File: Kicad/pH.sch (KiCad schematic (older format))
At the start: 6 parts, among them U1 MCP6241

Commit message: Ready for Rev3 First layout review
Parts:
- removed TP17, TP18: CONN_1, symbol CONN_1
- added C3: .1, ~, symbol C
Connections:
- net AGND: now also C3.2
- net V+_WallWart renamed V+_Clean
- net V+_Clean: now also C3.1
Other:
- note added: "Added .1uF"
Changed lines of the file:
@@
 $Descr A4 11693 8268
 encoding utf-8
-Sheet 7 7
+Sheet 6 7
 Title ""
-Date "11 oct 2014"
+Date "18 oct 2014"
 Rev ""
 Comp ""
@@
 Comment4 ""
 $EndDescr
-Text HLabel 3900 2400 0    60   Input ~ 0
+Text HLabel 1400 1200 0    60   Input ~ 0
 V+_WallWart
 Text HLabel 1350 3200 0    60   Input ~ 0
@@
 	1    0    0    -1
 $EndComp
-Wire Wire Line
-	3900 2900 3900 2400
 $Comp
 L CONN_1 TP1
@@
 Wire Wire Line
 	7450 3200 7450 3600
-Text HLabel 7450 2450 0    60   Input ~ 0
-V+_WallWart
-Wire Wire Line
-	7450 2700 7450 2450
 Text HLabel 5700 3100 2    60   Input ~ 0
 pH_Probe_V
@@
 Text HLabel 8600 3400 2    60   Input ~ 0
 pH_Probe_GND
-$Comp
-L CONN_1 TP18
-U 1 1 540C941C
-P 8500 2900
-F 0 "TP18" H 8580 2900 40  0000 L CNN
-F 1 "CONN_1" H 8500 2955 30  0001 C CNN
-F 2 "" H 8500 2900 60  0000 C CNN
-F 3 "" H 8500 2900 60  0000 C CNN
-	1    8500 2900
-	1    0    0    -1
-$EndComp
 Wire Wire Line
 	8050 1900 8050 3400
-$Comp
-L CONN_1 TP17
-U 1 1 540C9446
-P 5150 2750
-F 0 "TP17" H 5230 2750 40  0000 L CNN
-F 1 "CONN_1" H 5150 2805 30  0001 C CNN
-F 2 "" H 5150 2750 60  0000 C CNN
-F 3 "" H 5150 2750 60  0000 C CNN
-	1    5150 2750
-	0    -1   -1   0
-$EndComp
-Wire Wire Line
-	5150 2900 5150 3100
-Connection ~ 5150 3100
 Wire Wire Line
 	8050 1900 7950 1900
@@
 Connection ~ 7450 3400
 Connection ~ 8050 3400
+$Comp
+L C C3
+U 1 1 5441038F
+P 2000 1650
+F 0 "C3" H 2000 1750 40  0000 L CNN
+F 1 ".1" H 2006 1565 40  0000 L CNN
+F 2 "~" H 2038 1500 30  0000 C CNN
+F 3 "~" H 2000 1650 60  0000 C CNN
+	1    2000 1650
+	1    0    0    -1
+$EndComp
 Wire Wire Line
-	8350 2900 8350 3400
-Connection ~ 8350 3400
+	5950 2450 7450 2450
+Text Notes 1850 1050 0    60   ~ 0
+Added .1uF
+Wire Wire Line
+	1400 1200 2750 1200
+Wire Wire Line
+	2000 1450 2000 1200
+Connection ~ 2000 1200
+$Comp
+L AGND #PWR09
+U 1 1 5441062F
+P 2000 2050
+F 0 "#PWR09" H 2000 2050 40  0001 C CNN
+F 1 "AGND" H 2000 1980 50  0000 C CNN
+F 2 "" H 2000 2050 60  0000 C CNN
+F 3 "" H 2000 2050 60  0000 C CNN
+	1    2000 2050
+	1    0    0    -1
+$EndComp
+Wire Wire Line
+	2000 1850 2000 2050
+Wire Wire Line
+	3900 2900 3900 2400
+Wire Wire Line
+	7450 2450 7450 2700
+Text GLabel 2750 1200 2    60   Output ~ 0
+V+_Clean
+Text GLabel 3900 2400 2    60   Output ~ 0
+V+_Clean
+Text GLabel 6100 2300 2    60   Output ~ 0
+V+_Clean
+Wire Wire Line
+	5950 2450 5950 2300
+Wire Wire Line
+	5950 2300 6100 2300
 $EndSCHEMATC

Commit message: updated based on feedback. Ready for second review
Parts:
- removed C3: .1, ~, symbol C
- added C10, C9: .1, ~, symbol C
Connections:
- net labels removed: V+_Clean
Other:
- note removed: "Added .1uF"
- moved on the sheet: R3, R4
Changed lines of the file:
@@
 Sheet 6 7
 Title ""
-Date "18 oct 2014"
+Date "21 oct 2014"
 Rev ""
 Comp ""
@@
 Comment4 ""
 $EndDescr
-Text HLabel 1400 1200 0    60   Input ~ 0
-V+_WallWart
 Text HLabel 1350 3200 0    60   Input ~ 0
 ph_ADC_IN+
-Wire Wire Line
-	3900 3500 3900 3750
 $Comp
 L R R4
 U 1 1 53D7D158
-P 7450 3850
-F 0 "R4" V 7530 3850 40  0000 C CNN
-F 1 "1K" V 7457 3851 40  0000 C CNN
-F 2 "~" V 7380 3850 30  0000 C CNN
-F 3 "~" H 7450 3850 30  0000 C CNN
-	1    7450 3850
+P 8400 3900
+F 0 "R4" V 8480 3900 40  0000 C CNN
+F 1 "1K" V 8407 3901 40  0000 C CNN
+F 2 "~" V 8330 3900 30  0000 C CNN
+F 3 "~" H 8400 3900 30  0000 C CNN
+	1    8400 3900
 	1    0    0    -1
 $EndComp
-Wire Wire Line
-	1350 3200 3450 3200
-Text HLabel 7950 1900 0    60   Input ~ 0
+Text HLabel 8900 1950 0    60   Input ~ 0
 pH_ADC_IN-
 $Comp
-L AGND #PWR07
+L AGND #PWR08
 U 1 1 53DCC7DA
 P 3900 3750
-F 0 "#PWR07" H 3900 3750 40  0001 C CNN
+F 0 "#PWR08" H 3900 3750 40  0001 C CNN
 F 1 "AGND" H 3900 3680 50  0000 C CNN
 F 2 "" H 3900 3750 60  0000 C CNN
@@
 L R R3
 U 1 1 53F37946
-P 7450 2950
-F 0 "R3" V 7530 2950 40  0000 C CNN
-F 1 "10K" V 7457 2951 40  0000 C CNN
-F 2 "~" V 7380 2950 30  0000 C CNN
-F 3 "~" H 7450 2950 30  0000 C CNN
-	1    7450 2950
+P 8400 3000
+F 0 "R3" V 8480 3000 40  0000 C CNN
+F 1 "10K" V 8407 3001 40  0000 C CNN
+F 2 "~" V 8330 3000 30  0000 C CNN
+F 3 "~" H 8400 3000 30  0000 C CNN
+	1    8400 3000
 	1    0    0    -1
 $EndComp
@@
 	0    -1   -1   0
 $EndComp
+Text HLabel 5700 3100 2    60   Input ~ 0
+pH_Probe_V
+$Comp
+L AGND #PWR09
+U 1 1 540C92AB
+P 8400 4450
+F 0 "#PWR09" H 8400 4450 40  0001 C CNN
+F 1 "AGND" H 8400 4380 50  0000 C CNN
+F 2 "" H 8400 4450 60  0000 C CNN
+F 3 "" H 8400 4450 60  0000 C CNN
+	1    8400 4450
+	1    0    0    -1
+$EndComp
+Text HLabel 9550 3450 2    60   Input ~ 0
+pH_Probe_GND
+$Comp
+L C C9
+U 1 1 54453E50
+P 3550 2700
+F 0 "C9" H 3550 2800 40  0000 L CNN
+F 1 ".1" H 3556 2615 40  0000 L CNN
+F 2 "~" H 3588 2550 30  0000 C CNN
+F 3 "~" H 3550 2700 60  0000 C CNN
+	1    3550 2700
+	1    0    0    -1
+$EndComp
+Text HLabel 3900 2300 0    60   Input ~ 0
+V+_WallWart
+$Comp
+L AGND #PWR010
+U 1 1 54453F29
+P 3550 2900
+F 0 "#PWR010" H 3550 2900 40  0001 C CNN
+F 1 "AGND" H 3550 2830 50  0000 C CNN
+F 2 "" H 3550 2900 60  0000 C CNN
+F 3 "" H 3550 2900 60  0000 C CNN
+	1    3550 2900
+	1    0    0    -1
+$EndComp
+Wire Wire Line
+	3900 3500 3900 3750
+Wire Wire Line
+	1350 3200 3450 3200
 Wire Wire Line
 	2350 3050 2350 3200
 Connection ~ 2350 3200
 Wire Wire Line
-	7450 3200 7450 3600
-Text HLabel 5700 3100 2    60   Input ~ 0
-pH_Probe_V
+	8400 3250 8400 3650
 Wire Wire Line
 	4150 3100 5700 3100
@@
 	4750 3300 4150 3300
 Connection ~ 2950 3200
+Wire Wire Line
+	8400 4450 8400 4150
+Wire Wire Line
+	9000 1950 9000 3450
+Wire Wire Line
+	9000 1950 8900 1950
+Wire Wire Line
+	8400 3450 9550 3450
+Connection ~ 8400 3450
+Connection ~ 9000 3450
+Wire Wire Line
+	3900 2300 3900 2900
+Wire Wire Line
+	8400 2500 8400 2750
+Wire Wire Line
+	3550 2500 3550 2450
+Wire Wire Line
+	3550 2450 3900 2450
+Connection ~ 3900 2450
+Wire Wire Line
+	3550 2800 3550 2900
 $Comp
-L AGND #PWR08
-U 1 1 540C92AB
-P 7450 4400
-F 0 "#PWR08" H 7450 4400 40  0001 C CNN
-F 1 "AGND" H 7450 4330 50  0000 C CNN
-F 2 "" H 7450 4400 60  0000 C CNN
-F 3 "" H 7450 4400 60  0000 C CNN
-	1    7450 4400
+L C C10
+U 1 1 54453F94
+P 7750 2950
+F 0 "C10" H 7750 3050 40  0000 L CNN
+F 1 ".1" H 7756 2865 40  0000 L CNN
+F 2 "~" H 7788 2800 30  0000 C CNN
+F 3 "~" H 7750 2950 60  0000 C CNN
+	1    7750 2950
 	1    0    0    -1
 $EndComp
 Wire Wire Line
-	7450 4400 7450 4100
-Text HLabel 8600 3400 2    60   Input ~ 0
-pH_Probe_GND
-Wire Wire Line
-	8050 1900 8050 3400
-Wire Wire Line
-	8050 1900 7950 1900
-Wire Wire Line
-	7450 3400 8600 3400
-Connection ~ 7450 3400
-Connection ~ 8050 3400
+	7750 2750 7750 2500
 $Comp
-L C C3
-U 1 1 5441038F
-P 2000 1650
-F 0 "C3" H 2000 1750 40  0000 L CNN
-F 1 ".1" H 2006 1565 40  0000 L CNN
-F 2 "~" H 2038 1500 30  0000 C CNN
-F 3 "~" H 2000 1650 60  0000 C CNN
-	1    2000 1650
+L AGND #PWR011
+U 1 1 54453FBC
+P 7750 3450
+F 0 "#PWR011" H 7750 3450 40  0001 C CNN
+F 1 "AGND" H 7750 3380 50  0000 C CNN
+F 2 "" H 7750 3450 60  0000 C CNN
+F 3 "" H 7750 3450 60  0000 C CNN
+	1    7750 3450
 	1    0    0    -1
 $EndComp
 Wire Wire Line
-	5950 2450 7450 2450
-Text Notes 1850 1050 0    60   ~ 0
-Added .1uF
+	7750 3450 7750 3150
+Text HLabel 7450 2500 0    60   Input ~ 0
+V+_WallWart
 Wire Wire Line
-	1400 1200 2750 1200
-Wire Wire Line
-	2000 1450 2000 1200
-Connection ~ 2000 1200
-$Comp
-L AGND #PWR09
-U 1 1 5441062F
-P 2000 2050
-F 0 "#PWR09" H 2000 2050 40  0001 C CNN
-F 1 "AGND" H 2000 1980 50  0000 C CNN
-F 2 "" H 2000 2050 60  0000 C CNN
-F 3 "" H 2000 2050 60  0000 C CNN
-	1    2000 2050
-	1    0    0    -1
-$EndComp
-Wire Wire Line
-	2000 1850 2000 2050
-Wire Wire Line
-	3900 2900 3900 2400
-Wire Wire Line
-	7450 2450 7450 2700
-Text GLabel 2750 1200 2    60   Output ~ 0
-V+_Clean
-Text GLabel 3900 2400 2    60   Output ~ 0
-V+_Clean
-Text GLabel 6100 2300 2    60   Output ~ 0
-V+_Clean
-Wire Wire Line
-	5950 2450 5950 2300
-Wire Wire Line
-	5950 2300 6100 2300
+	7450 2500 8400 2500
+Connection ~ 7750 2500
 $EndSCHEMATC

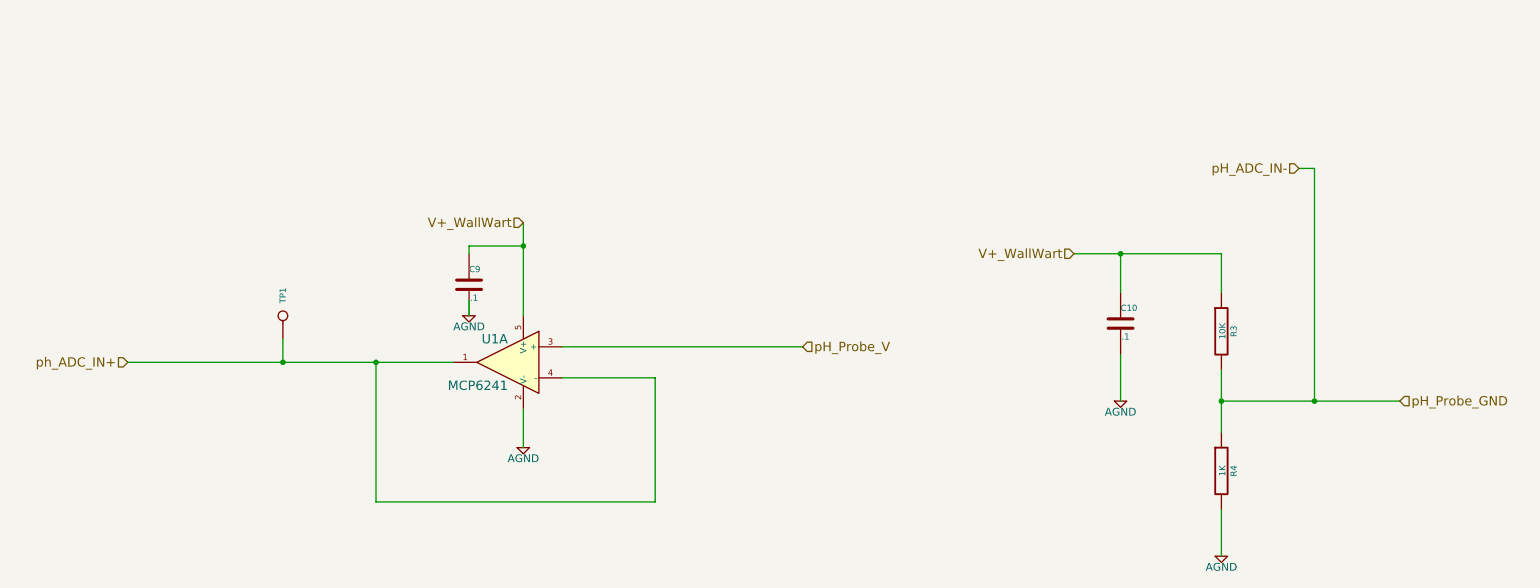
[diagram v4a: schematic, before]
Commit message: first pass changing ADC
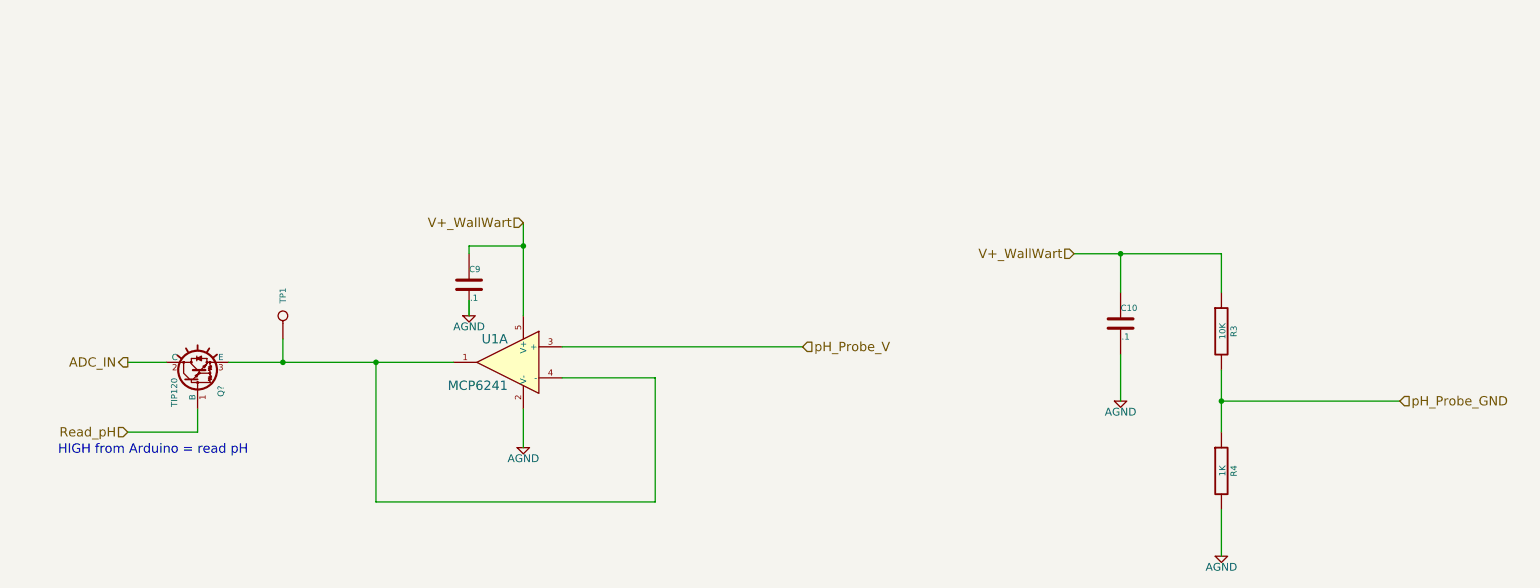
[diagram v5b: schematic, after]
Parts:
- added Q?: TIP120, TO220, symbol TIP120
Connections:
- net labels added: ADC_IN, Read_pH
- net labels removed: pH_ADC_IN-, ph_ADC_IN+
- wire segments 21 -> 22
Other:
- note added: "HIGH from Arduino = read pH"
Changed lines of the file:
@@
 Sheet 5 7
 Title ""
-Date "10 nov 2014"
+Date "11 nov 2014"
 Rev ""
 Comp ""
@@
 Comment4 ""
 $EndDescr
-Text HLabel 1350 3200 0    60   Input ~ 0
-ph_ADC_IN+
+Text HLabel 1350 3200 0    60   Output ~ 0
+ADC_IN
 $Comp
 L R R4
@@
 	1    0    0    -1
 $EndComp
-Text HLabel 8900 1950 0    60   Input ~ 0
-pH_ADC_IN-
 $Comp
 L AGND #PWR08
@@
 	3900 3500 3900 3750
 Wire Wire Line
-	1350 3200 3450 3200
-Wire Wire Line
 	2350 3050 2350 3200
-Connection ~ 2350 3200
 Wire Wire Line
 	8400 3250 8400 3650
 Wire Wire Line
 	4150 3100 5700 3100
-Wire Wire Line
-	2950 3200 2950 4100
 Wire Wire Line
 	2950 4100 4750 4100
@@
 Wire Wire Line
 	4750 3300 4150 3300
-Connection ~ 2950 3200
 Wire Wire Line
 	8400 4450 8400 4150
 Wire Wire Line
-	9000 1950 9000 3450
-Wire Wire Line
-	9000 1950 8900 1950
-Wire Wire Line
 	8400 3450 9550 3450
 Connection ~ 8400 3450
-Connection ~ 9000 3450
 Wire Wire Line
 	3900 2300 3900 2900
@@
 	7450 2500 8400 2500
 Connection ~ 7750 2500
+$Comp
+L TIP120 Q?
+U 1 1 54622290
+P 1800 3300
+F 0 "Q?" H 1750 3150 40  0000 R CNN
+F 1 "TIP120" H 1800 3450 40  0000 R CNN
+F 2 "TO220" H 1680 3405 29  0001 C CNN
+F 3 "~" H 1800 3300 60  0000 C CNN
+	1    1800 3300
+	0    -1   -1   0
+$EndComp
+Wire Wire Line
+	2000 3200 3450 3200
+Connection ~ 2350 3200
+Wire Wire Line
+	1600 3200 1350 3200
+Wire Wire Line
+	1800 3650 1800 3500
+Text HLabel 1350 3650 0    60   Input ~ 0
+Read_pH
+Wire Wire Line
+	1350 3650 1800 3650
+Wire Wire Line
+	2950 4100 2950 3200
+Connection ~ 2950 3200
+Text Notes 900  3800 0    60   ~ 0
+HIGH from Arduino = read pH
 $EndSCHEMATC

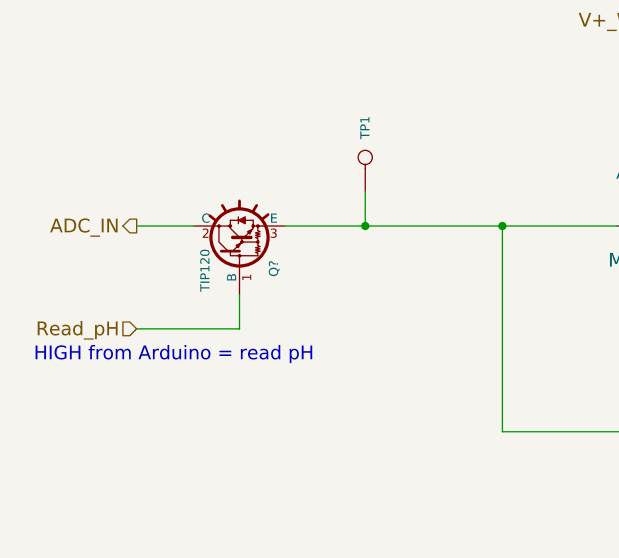
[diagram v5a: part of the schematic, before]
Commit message: prior to using Arduino ADC
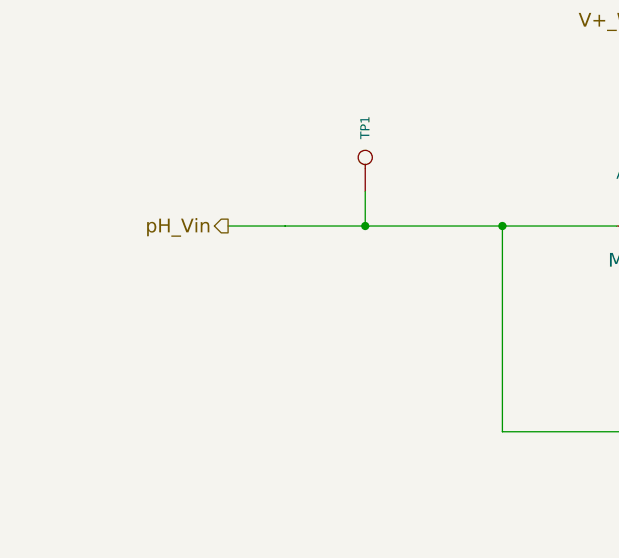
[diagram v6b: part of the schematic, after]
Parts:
- removed Q?: TIP120, TO220, symbol TIP120
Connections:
- net labels added: pH_Vin
- net labels removed: ADC_IN, Read_pH
- wire segments 22 -> 20
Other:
- note removed: "HIGH from Arduino = read pH"
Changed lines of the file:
@@
 $Descr A4 11693 8268
 encoding utf-8
-Sheet 5 7
+Sheet 7 7
 Title ""
-Date "11 nov 2014"
+Date "12 nov 2014"
 Rev ""
 Comp ""
@@
 Comment4 ""
 $EndDescr
-Text HLabel 1350 3200 0    60   Output ~ 0
-ADC_IN
+Text HLabel 1750 3200 0    60   Output ~ 0
+pH_Vin
 $Comp
 L R R4
@@
 	7450 2500 8400 2500
 Connection ~ 7750 2500
-$Comp
-L TIP120 Q?
-U 1 1 54622290
-P 1800 3300
-F 0 "Q?" H 1750 3150 40  0000 R CNN
-F 1 "TIP120" H 1800 3450 40  0000 R CNN
-F 2 "TO220" H 1680 3405 29  0001 C CNN
-F 3 "~" H 1800 3300 60  0000 C CNN
-	1    1800 3300
-	0    -1   -1   0
-$EndComp
 Wire Wire Line
 	2000 3200 3450 3200
 Connection ~ 2350 3200
 Wire Wire Line
-	1600 3200 1350 3200
-Wire Wire Line
-	1800 3650 1800 3500
-Text HLabel 1350 3650 0    60   Input ~ 0
-Read_pH
-Wire Wire Line
-	1350 3650 1800 3650
+	2000 3200 1750 3200
 Wire Wire Line
 	2950 4100 2950 3200
 Connection ~ 2950 3200
-Text Notes 900  3800 0    60   ~ 0
-HIGH from Arduino = read pH
 $EndSCHEMATC
